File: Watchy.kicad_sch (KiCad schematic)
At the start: 56 parts, among them J1 FPC24(0.5MM), J2 Micro USB, J3 Battery, M1 Vibration_Motor, Q1 AO3400A, Q2 UMH3N, Q4 CJ2301, Q5 S8050, SW1 BTN, SW2 BTN, SW3 BTN, SW4 BTN, U1 ESP32-PICO-D4, U2 ME6211C33M5G-N, U3 CP2104, U4 BMA423, U5 TP4054, U6 DS3231MZ, U7 BMA423

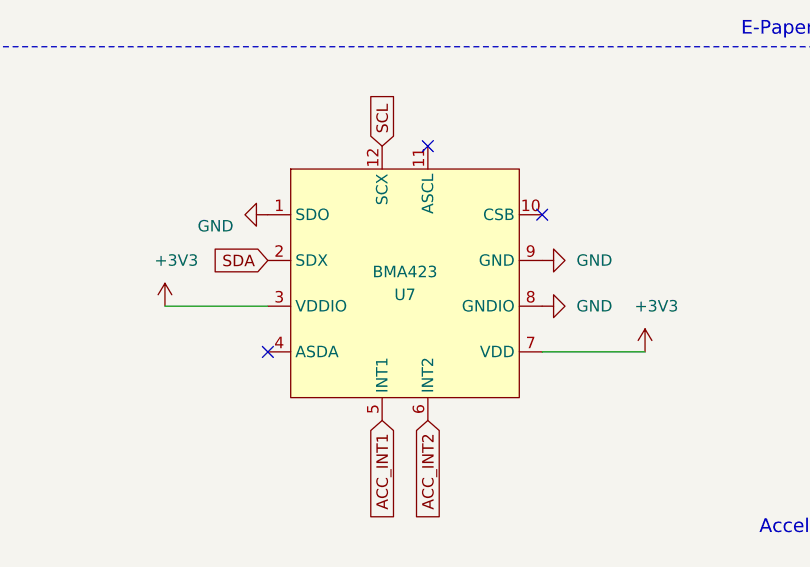
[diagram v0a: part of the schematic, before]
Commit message: add project-specific symbol field names (Manufacturer, part number, ..)
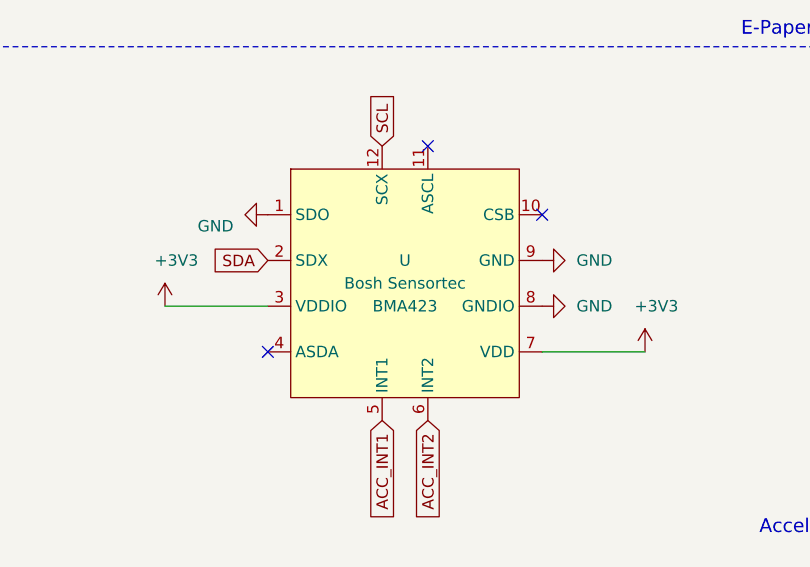
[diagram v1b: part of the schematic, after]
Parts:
- removed U7: BMA423, symbol Watchy:BMA423
- added U: BMA423, symbol Watchy:BMA423
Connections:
- net +3V3: now also U.3 (VDDIO), U.7 (VDD)
- net ACC_INT1: now also U.5 (INT1)
- net ACC_INT2: now also U.6 (INT2)
- net GND: now also U.1 (SDO), U.8 (GNDIO), U.9 (GND)
- net SCL: now also U.12 (SCX)
- net SDA: now also U.2 (SDX)
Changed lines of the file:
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@@
   (symbol (lib_name "Watchy:BMA423_1") (lib_id "Watchy:BMA423") (at 228.6 137.16 0) (unit 1)
     (in_bom yes) (on_board yes)
-    (property "Reference" "U7" (id 0) (at 228.6 138.43 0))
-    (property "Value" "BMA423" (id 1) (at 228.6 135.89 0))
+    (property "Reference" "U" (id 0) (at 228.6 134.62 0))
+    (property "Value" "BMA423" (id 1) (at 228.6 139.7 0))
     (property "Footprint" "" (id 2) (at 224.79 137.16 0)
       (effects (font (size 1.27 1.27)) hide)
     )
-    (property "Datasheet" "" (id 3) (at 224.79 137.16 0)
+    (property "Datasheet" "https://www.bosch-sensortec.com/media/boschsensortec/downloads/datasheets/bst-bma423-ds004-00.pdf" (id 3) (at 224.79 137.16 0)
+      (effects (font (size 1.27 1.27)) hide)
+    )
+    (property "Manufacturer" "Bosh Sensortec" (id 4) (at 228.6 137.16 0))
+    (property "Manufacturer Part Number" "BMA423" (id 4) (at 228.6 137.16 0)
+      (effects (font (size 1.27 1.27)) hide)
+    )
+    (property "Digikey Part Number" "828-1075-1-ND" (id 5) (at 228.6 137.16 0)
+      (effects (font (size 1.27 1.27)) hide)
+    )
+    (property "Digikey Link" "https://www.digikey.fi/product-detail/fi/bosch-sensortec/BMA456/828-1075-1-ND/7401320" (id 6) (at 228.6 137.16 0)
       (effects (font (size 1.27 1.27)) hide)
     )
@@
       (reference "SW4") (unit 1) (value "BTN") (footprint "Watchy:K2-1114SA-A4SW-06")
     )
+    (path "/5fa582e0-f11f-4eca-9bdf-0ceb430d3a95"
+      (reference "U") (unit 1) (value "BMA423") (footprint "")
+    )
     (path "/00000000-0000-0000-0000-00005df2a49b"
       (reference "U1") (unit 1) (value "ESP32-PICO-D4") (footprint "Housings_DFN_QFN:QFN-48-1EP_7x7mm_Pitch0.5mm")
@@
       (reference "U6") (unit 1) (value "DS3231MZ") (footprint "Housings_SOIC:SOIC-8_3.9x4.9mm_Pitch1.27mm")
     )
-    (path "/4aaf9105-6407-4df5-bb82-4814ac567ad8"
-      (reference "U7") (unit 1) (value "BMA423") (footprint "")
-    )
   )
